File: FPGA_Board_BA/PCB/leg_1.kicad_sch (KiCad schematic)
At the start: 4 parts, among them Q5 IPT017N12NM6, Q6 IPT017N12NM6

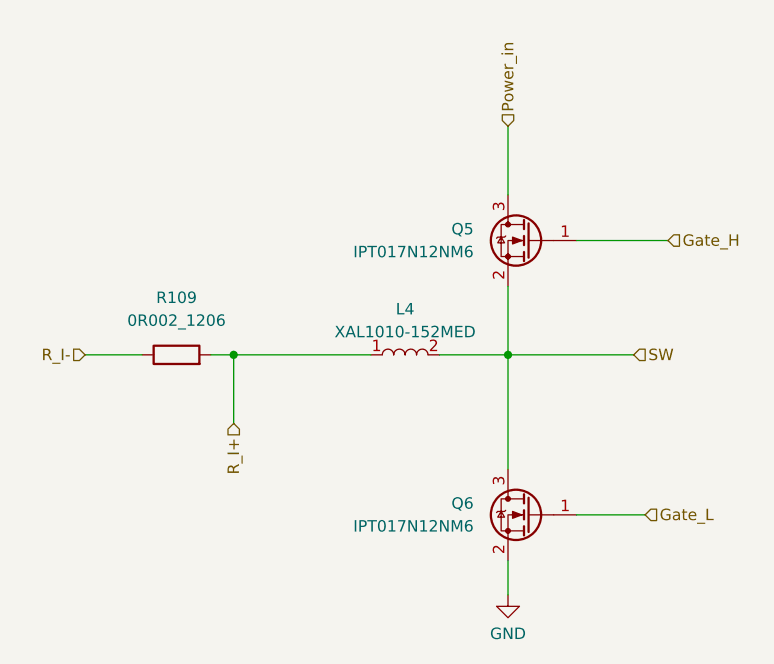
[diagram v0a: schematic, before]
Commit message: component placement with new concept is ready
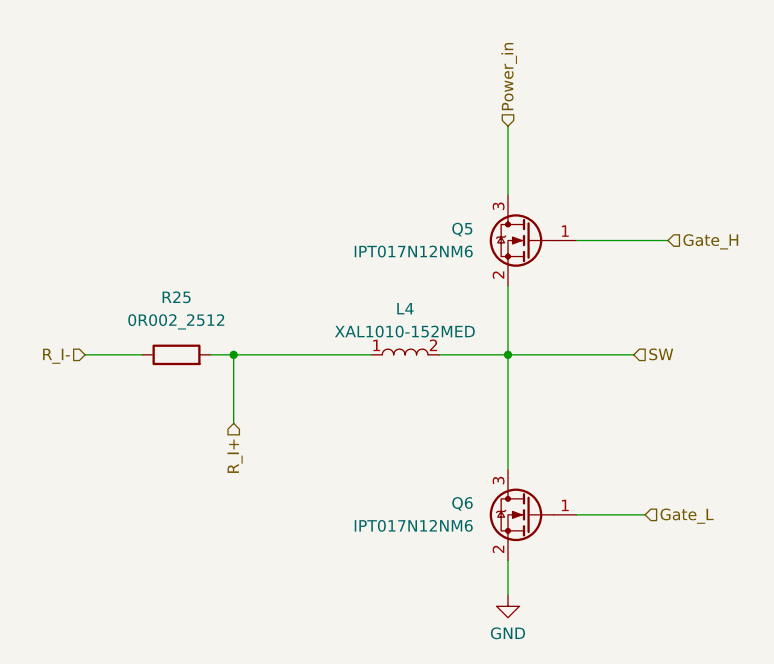
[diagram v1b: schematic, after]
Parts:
- removed R109: 0R002_1206, Resistor_SMD:R_1206_3216Metric_Pad1.30x1.75mm_HandSolder, symbol MYLIB_Misc:0R002_1206
- added R25: 0R002_2512, Resistor_SMD:R_2512_6332Metric, symbol MYLIB_Misc:0R002_2512
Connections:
- net R_I+: now also R25.2
- net R_I-: now also R25.1
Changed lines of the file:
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@@
-	)
-	(symbol
-		(lib_id "MYLIB_Misc:0R002_1206")
-		(at 110.49 105.41 90)
-		(unit 1)
-		(exclude_from_sim no)
-		(in_bom yes)
-		(on_board yes)
-		(dnp no)
-		(fields_autoplaced yes)
-		(property "Reference" "R109"
-			(at 110.49 99.06 90)
-			(effects
-				(font
-					(size 1.27 1.27)
-				)
-			)
-		)
-		(property "Value" "0R002_1206"
-			(at 110.49 101.6 90)
-			(effects
-				(font
-					(size 1.27 1.27)
-				)
-			)
-		)
-		(property "Footprint" "Resistor_SMD:R_1206_3216Metric_Pad1.30x1.75mm_HandSolder"
-			(at 89.662 104.902 0)
-			(effects
-				(font
-					(size 1.27 1.27)
-				)
-				(hide yes)
-			)
-		)
-		(property "Datasheet" "https://eu.mouser.com/datasheet/3/1099/1/SEI-CSNL.pdf"
-			(at 92.71 104.648 0)
-			(effects
-				(font
-					(size 1.27 1.27)
-				)
-				(hide yes)
-			)
-		)
-		(property "Description" "2mOhm, 1W, 1% Shunt Resistor"
-			(at 96.266 105.41 0)
-			(effects
-				(font
-					(size 1.27 1.27)
-				)
-				(hide yes)
-			)
-		)
-		(property "Mouser nr" " 708-CSNL1206FT2L00 "
-			(at 98.298 105.664 0)
-			(effects
-				(font
-					(size 1.27 1.27)
-				)
-				(hide yes)
-			)
-		)
-		(pin "2"
-		)
-		(pin "1"
-		)
-		(instances
-			(project "FPGA_Board_BA"
-				(path "/fd7503bc-e7fc-4766-b224-3d1c3d7de5ff/c363a192-a091-4a49-a77c-8a6e46625814/a8143cfd-ddb3-4057-8e4e-552f3aa79edb"
-					(reference "R109")
-					(unit 1)
-				)
-				(path "/fd7503bc-e7fc-4766-b224-3d1c3d7de5ff/c363a192-a091-4a49-a77c-8a6e46625814/b09ceb72-5b70-4bc2-a2af-bf1e7fddc9a1"
-					(reference "R1")
-					(unit 1)
-				)
-			)
-		)
 	)
 	(symbol
@@
 					(unit 1)
 				)
+			)
+		)
+	)
+	(symbol
+		(lib_id "MYLIB_Misc:0R002_2512")
+		(at 110.49 105.41 90)
+		(unit 1)
+		(exclude_from_sim no)
+		(in_bom yes)
+		(on_board yes)
+		(dnp no)
+		(fields_autoplaced yes)
+		(property "Reference" "R25"
+			(at 110.49 99.06 90)
+			(effects
+				(font
+					(size 1.27 1.27)
+				)
+			)
+		)
+		(property "Value" "0R002_2512"
+			(at 110.49 101.6 90)
+			(effects
+				(font
+					(size 1.27 1.27)
+				)
+			)
+		)
+		(property "Footprint" "Resistor_SMD:R_2512_6332Metric"
+			(at 95.25 105.918 0)
+			(effects
+				(font
+					(size 1.27 1.27)
+				)
+				(hide yes)
+			)
+		)
+		(property "Datasheet" "https://eu.mouser.com/datasheet/3/1099/1/SEI-CSNL.pdf"
+			(at 90.17 104.648 0)
+			(effects
+				(font
+					(size 1.27 1.27)
+				)
+				(hide yes)
+			)
+		)
+		(property "Description" "Shunt Resistor 3W, 2512"
+			(at 92.964 105.664 0)
+			(effects
+				(font
+					(size 1.27 1.27)
+				)
+				(hide yes)
+			)
+		)
+		(property "Mouser nr" "708-CSNL2512FT2L00 "
+			(at 98.044 105.156 0)
+			(effects
+				(font
+					(size 1.27 1.27)
+				)
+				(hide yes)
+			)
+		)
+		(pin "2"
+		)
+		(pin "1"
+		)
+		(instances
+			(project ""
+				(path "/fd7503bc-e7fc-4766-b224-3d1c3d7de5ff/c363a192-a091-4a49-a77c-8a6e46625814/a8143cfd-ddb3-4057-8e4e-552f3aa79edb"
+					(reference "R25")
+					(unit 1)
+				)
+				(path "/fd7503bc-e7fc-4766-b224-3d1c3d7de5ff/c363a192-a091-4a49-a77c-8a6e46625814/b09ceb72-5b70-4bc2-a2af-bf1e7fddc9a1"
+					(reference "R26")
+					(unit 1)
+				)
